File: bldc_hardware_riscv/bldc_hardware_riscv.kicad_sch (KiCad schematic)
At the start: 31 parts, among them J1 USB_B_Micro, J2 Screw_Terminal_01x06, J3 Screw_Terminal_01x06, U1 CH32V307VCT6

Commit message: First release to PCB manufacture
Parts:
- added AE1: (no value), symbol Device:Antenna
- added C39, C40: 0.1uF, Capacitor_SMD:C_0603_1608Metric, symbol Device:C
- added U8: (no value), symbol BLDC_Library:CH9141K
- added Y2: Crystal_GND24, BLDC_Library:Oscillator_SMD_Abracon_ASE-4Pin_3.2x2.5mm, symbol Device:Crystal_GND24
- D14, D15: value (none) -> LED; footprint (none) -> LED_SMD:LED_0603_1608Metric
- J4: renamed from J?; value (none) -> Screw_Terminal_01x04; footprint (none) -> Connector_PinHeader_2.54mm:PinHeader_1x04_P2.54mm_Vertical
- R1: value (none) -> 10K; footprint (none) -> Resistor_SMD:R_0603_1608Metric
- R38: value (none) -> 1K; footprint (none) -> Resistor_SMD:R_0603_1608Metric
- R39: value (none) -> 1K
- U7: value (none) -> SN65HVD230; footprint (none) -> Package_SO:SOIC-8_3.9x4.9mm_P1.27mm
- Y1: value (none) -> Crystal_GND24; footprint (none) -> BLDC_Library:Oscillator_SMD_Abracon_ASE-4Pin_3.2x2.5mm
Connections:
- net SWID is gone; now on net SWIO: U1.72 (PA13/SWDIO)
- net 3.3V: now also C39.1, U8.2 (VCC)
- net GND: now also AE1.1 (A), C39.2, C40.2, U8.11 (GND), U8.3 (GND), U8.6 (ANT), Y2.2, Y2.4
- net BLE_MODE: now reaches U1.38 (PE7)
- net BLE_MODE: now also U8.10 (AT)
- net BLE_TX: now reaches U1.45 (PE14)
- net BLE_TX: now also U8.8 (RXD)
- net BLE_RX: now reaches U1.46 (PE15)
- net BLE_RX: now also U8.9 (TXD)
- new net: C40.1, U8.7 (VA)
- new net: U8.4 (XI), Y2.1
- new net: U8.5 (XO), Y2.3

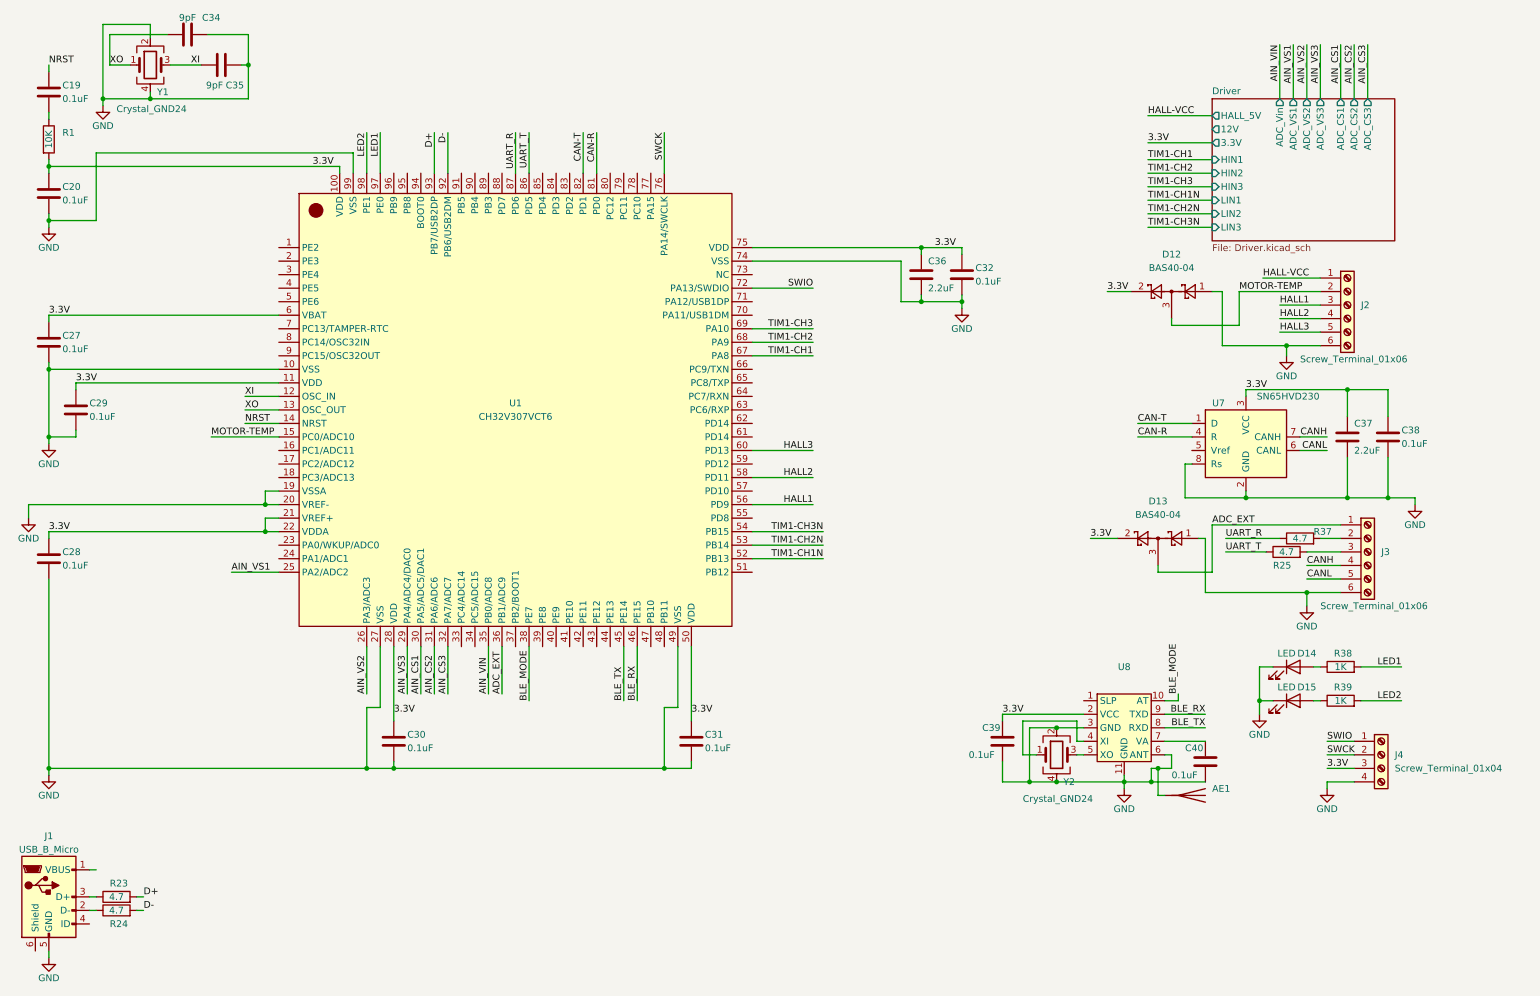
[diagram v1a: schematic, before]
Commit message: fix resistor/inductor/capacitor parameters, add boot button, add 120Ohm CAN bus load resistor.
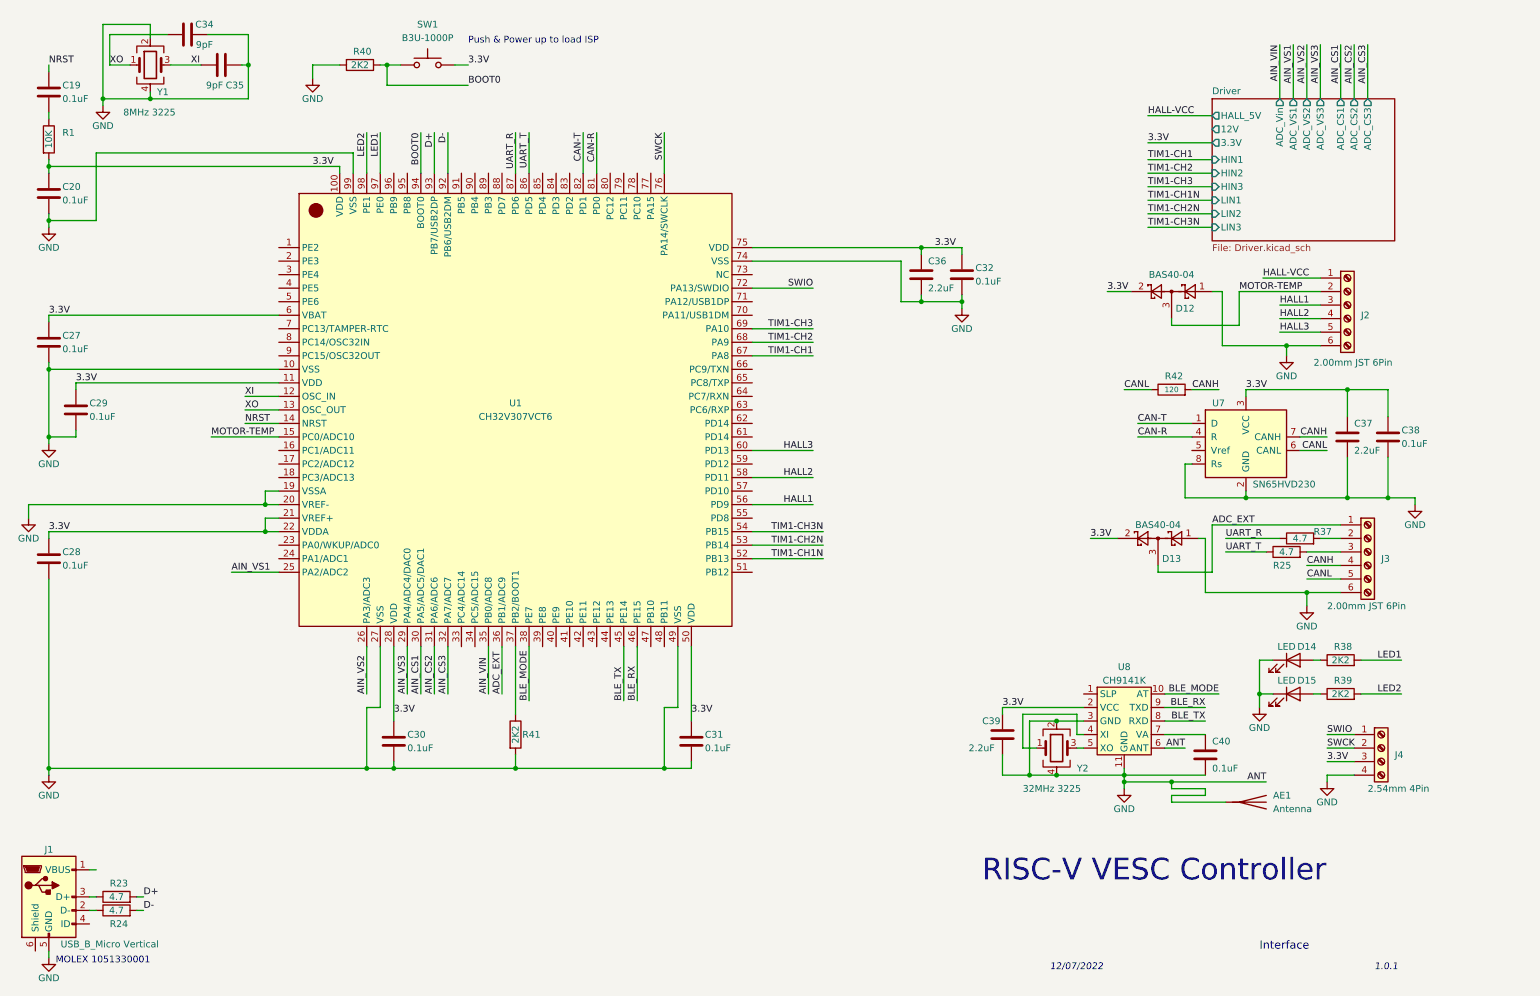
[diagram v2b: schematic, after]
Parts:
- added R40, R41: 2K2, Resistor_SMD:R_0603_1608Metric, symbol Device:R
- added R42: 120, Resistor_SMD:R_0805_2012Metric, symbol Device:R
- added SW1: B3U-1000P, Button_Switch_SMD:SW_SPST_B3U-1000P, symbol Switch:SW_Push
- AE1: value (none) -> Antenna; footprint (none) -> BLDC_Library:ANT-F-1-2.4G-0.6MM-FR4
- C39: value 0.1uF -> 2.2uF
- J1: value USB_B_Micro -> USB_B_Micro Vertical
- J2, J3: value Screw_Terminal_01x06 -> 2.00mm JST 6Pin
- J4: value Screw_Terminal_01x04 -> 2.54mm 4Pin
- R38, R39: value 1K -> 2K2
- U8: value (none) -> CH9141K; footprint (none) -> BLDC_Library:HSOP-10-1EP_3.9x4.9mm_P1.27mm_EP2.3x2.3mm
- Y1: value Crystal_GND24 -> 8MHz 3225
- Y2: value Crystal_GND24 -> 32MHz 3225
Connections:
- net 3.3V: now also SW1.2
- net CANH: now also R42.2
- net CANL: now also R42.1
- net GND: now also R40.2, R41.2
- net at U1.37 (PB2/BOOT1): now also R41.1
- net BOOT0: now reaches U1.94 (BOOT0)
- net BOOT0: now also R40.1, SW1.1
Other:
- note added: "1.0.1"
- note added: "12/07/2022"
- note added: "Interface"
- note added: "MOLEX 1051330001"
- note added: "Push & Power up to load ISP"
- note added: "RISC-V VESC Controller"
- moved on the sheet: AE1, C39, C40, D14, D15, J4, R38, R39, U8, Y2
